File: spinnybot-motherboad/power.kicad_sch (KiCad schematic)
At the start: 19 parts, among them J11 POWER SW2, J9 POWER SW1, Q1 SISA96DN, Q2 SISA96DN, Q4 Q_NMOS_DGS, U1 LM1117-3.3

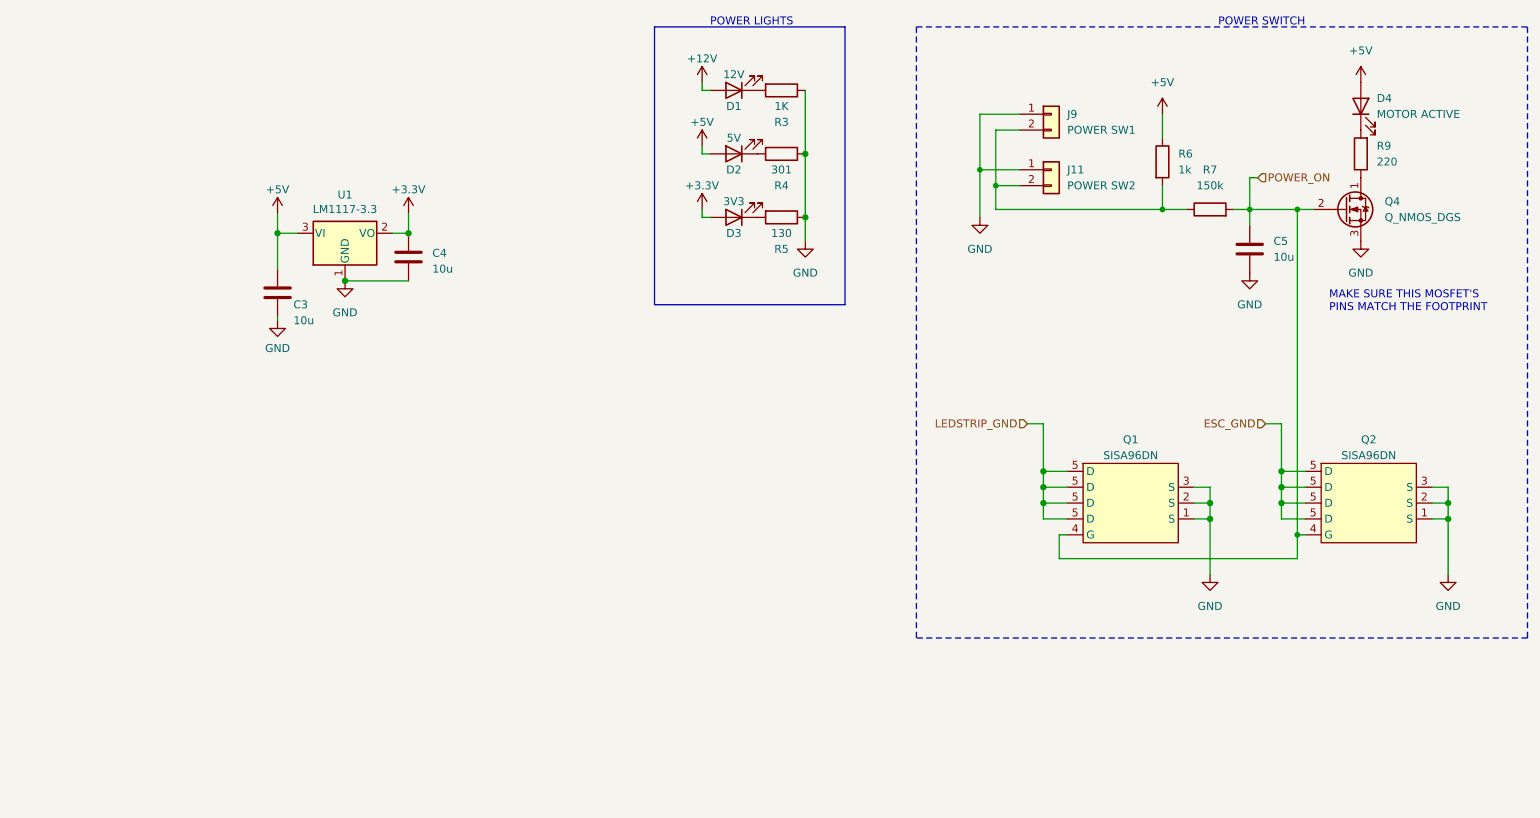
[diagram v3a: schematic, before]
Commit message: Power pads added, beginning routing
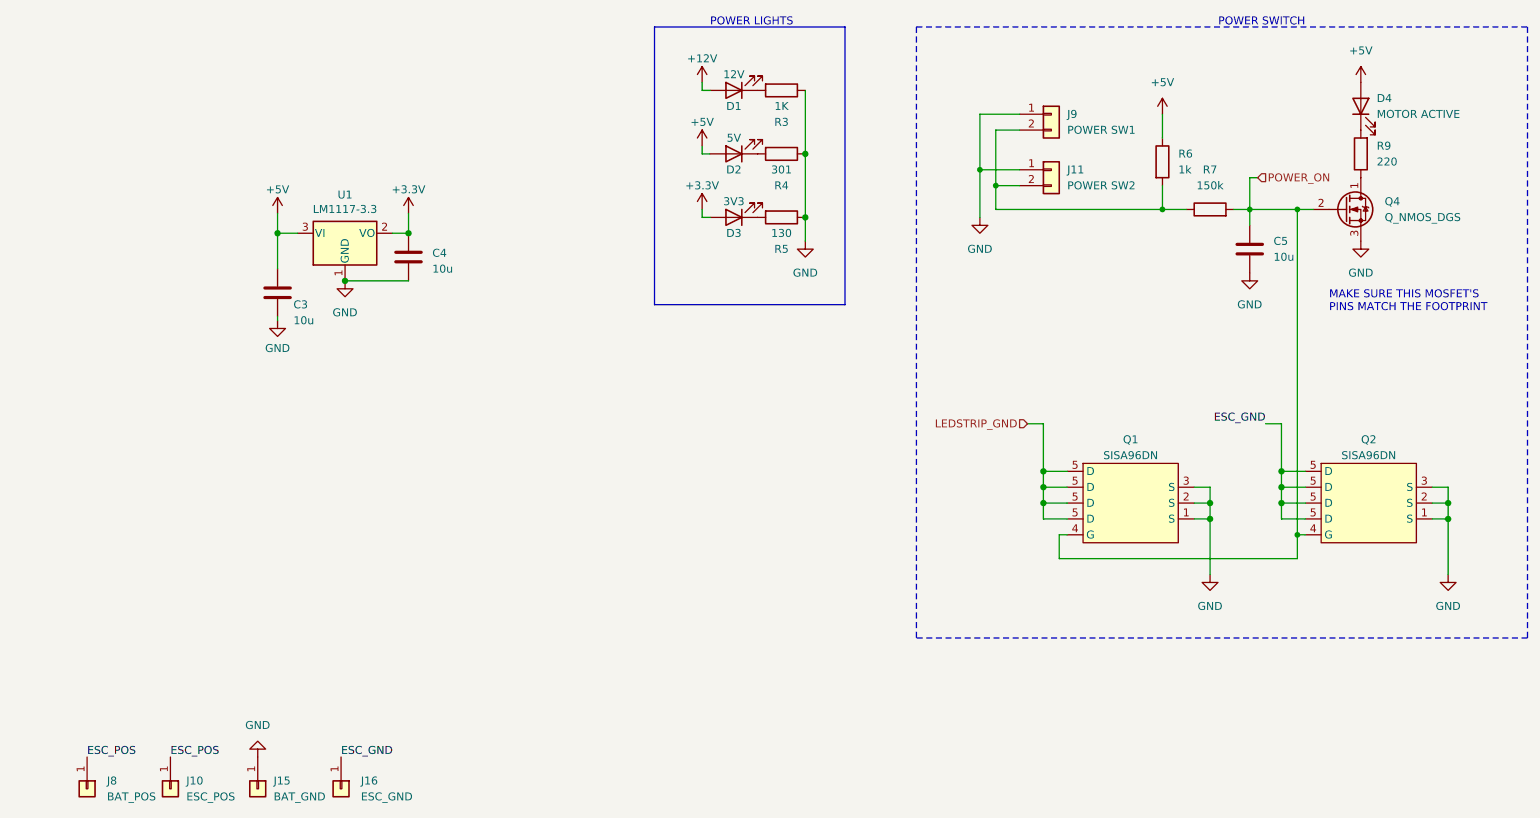
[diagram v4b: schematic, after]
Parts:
- added J10: ESC_POS, custom:Stitched_SolderWirePad_1x01_SMD_5x10mm, symbol Connector_Generic:Conn_01x01
- added J15: BAT_GND, custom:Stitched_SolderWirePad_1x01_SMD_5x10mm, symbol Connector_Generic:Conn_01x01
- added J16: ESC_GND, Connector_Wire:SolderWirePad_1x01_SMD_5x10mm, symbol Connector_Generic:Conn_01x01
- added J8: BAT_POS, Connector_Wire:SolderWirePad_1x01_SMD_5x10mm, symbol Connector_Generic:Conn_01x01
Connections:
- net ESC_GND: now also J16.1 (Pin_1)
- net GND: now also J15.1 (Pin_1)
- new net ESC_POS: J10.1 (Pin_1), J8.1 (Pin_1)
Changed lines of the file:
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@@
+    (effects (font (size 1.27 1.27)) (justify left bottom))
+  )
+  (label "ESC_POS" (at 40.005 134.62 0)
+    (effects (font (size 1.27 1.27)) (justify left bottom))
+  )
+  (label "ESC_GND" (at 80.645 134.62 0)
+    (effects (font (size 1.27 1.27)) (justify left bottom))
+  )
+  (label "ESC_GND" (at 228.6 81.28 180)
+    (effects (font (size 1.27 1.27)) (justify right bottom))
+  )
+  (label "ESC_POS" (at 53.34 134.62 0)
     (effects (font (size 1.27 1.27)) (justify left bottom))
   )
@@
     (effects (font (size 1.27 1.27)) (justify left))
   )
-  (hierarchical_label "ESC_GND" (shape input) (at 228.6 81.28 180)
-    (effects (font (size 1.27 1.27)) (justify right))
-  )
   (symbol (lib_id "power:GND") (at 219.71 105.41 0) (unit 1)
     (in_bom yes) (on_board yes)
@@
     )
     (property "Datasheet" "" (id 3) (at 70.485 47.625 0)
+      (effects (font (size 1.27 1.27)) hide)
+    )
+    (pin "1")
+  )
+  (symbol (lib_id "power:GND") (at 67.31 134.62 180) (unit 1)
+    (in_bom yes) (on_board yes) (fields_autoplaced)
+    (property "Reference" "#PWR0158" (id 0) (at 67.31 128.27 0)
+      (effects (font (size 1.27 1.27)) hide)
+    )
+    (property "Value" "GND" (id 1) (at 67.31 129.54 0))
+    (property "Footprint" "" (id 2) (at 67.31 134.62 0)
+      (effects (font (size 1.27 1.27)) hide)
+    )
+    (property "Datasheet" "" (id 3) (at 67.31 134.62 0)
+      (effects (font (size 1.27 1.27)) hide)
+    )
+    (pin "1")
+  )
+  (symbol (lib_id "Connector_Generic:Conn_01x01") (at 53.34 139.7 270) (unit 1)
+    (in_bom yes) (on_board yes) (fields_autoplaced)
+    (property "Reference" "J10" (id 0) (at 55.88 138.4299 90)
+      (effects (font (size 1.27 1.27)) (justify left))
+    )
+    (property "Value" "ESC_POS" (id 1) (at 55.88 140.9699 90)
+      (effects (font (size 1.27 1.27)) (justify left))
+    )
+    (property "Footprint" "custom:Stitched_SolderWirePad_1x01_SMD_5x10mm" (id 2) (at 53.34 139.7 0)
+      (effects (font (size 1.27 1.27)) hide)
+    )
+    (property "Datasheet" "~" (id 3) (at 53.34 139.7 0)
       (effects (font (size 1.27 1.27)) hide)
     )
@@
     )
     (property "Datasheet" "" (id 3) (at 212.09 31.75 0)
+      (effects (font (size 1.27 1.27)) hide)
+    )
+    (pin "1")
+  )
+  (symbol (lib_id "Connector_Generic:Conn_01x01") (at 67.31 139.7 270) (unit 1)
+    (in_bom yes) (on_board yes) (fields_autoplaced)
+    (property "Reference" "J15" (id 0) (at 69.85 138.4299 90)
+      (effects (font (size 1.27 1.27)) (justify left))
+    )
+    (property "Value" "BAT_GND" (id 1) (at 69.85 140.9699 90)
+      (effects (font (size 1.27 1.27)) (justify left))
+    )
+    (property "Footprint" "custom:Stitched_SolderWirePad_1x01_SMD_5x10mm" (id 2) (at 67.31 139.7 0)
+      (effects (font (size 1.27 1.27)) hide)
+    )
+    (property "Datasheet" "~" (id 3) (at 67.31 139.7 0)
       (effects (font (size 1.27 1.27)) hide)
     )
@@
     (pin "2")
   )
+  (symbol (lib_id "Connector_Generic:Conn_01x01") (at 40.005 139.7 270) (unit 1)
+    (in_bom yes) (on_board yes) (fields_autoplaced)
+    (property "Reference" "J8" (id 0) (at 43.18 138.4299 90)
+      (effects (font (size 1.27 1.27)) (justify left))
+    )
+    (property "Value" "BAT_POS" (id 1) (at 43.18 140.9699 90)
+      (effects (font (size 1.27 1.27)) (justify left))
+    )
+    (property "Footprint" "Connector_Wire:SolderWirePad_1x01_SMD_5x10mm" (id 2) (at 40.005 139.7 0)
+      (effects (font (size 1.27 1.27)) hide)
+    )
+    (property "Datasheet" "~" (id 3) (at 40.005 139.7 0)
+      (effects (font (size 1.27 1.27)) hide)
+    )
+    (pin "1")
+  )
   (symbol (lib_id "power:GND") (at 154.94 52.07 0) (unit 1)
     (in_bom yes) (on_board yes)
@@
     (pin "2")
   )
+  (symbol (lib_id "Connector_Generic:Conn_01x01") (at 80.645 139.7 270) (unit 1)
+    (in_bom yes) (on_board yes) (fields_autoplaced)
+    (property "Reference" "J16" (id 0) (at 83.82 138.4299 90)
+      (effects (font (size 1.27 1.27)) (justify left))
+    )
+    (property "Value" "ESC_GND" (id 1) (at 83.82 140.9699 90)
+      (effects (font (size 1.27 1.27)) (justify left))
+    )
+    (property "Footprint" "Connector_Wire:SolderWirePad_1x01_SMD_5x10mm" (id 2) (at 80.645 139.7 0)
+      (effects (font (size 1.27 1.27)) hide)
+    )
+    (property "Datasheet" "~" (id 3) (at 80.645 139.7 0)
+      (effects (font (size 1.27 1.27)) hide)
+    )
+    (pin "1")
+  )
   (symbol (lib_id "Device:C") (at 91.44 54.61 0) (unit 1)

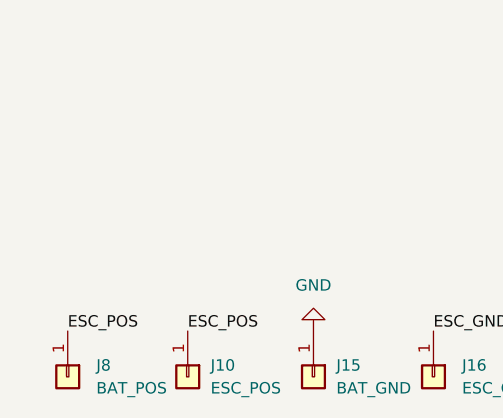
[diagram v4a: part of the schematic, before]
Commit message: Finishing routing board, needs checking over to make sure everything looks good
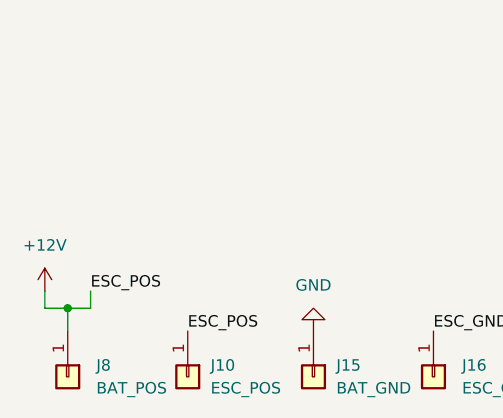
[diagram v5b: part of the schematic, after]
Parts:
- J11, J9: footprint Connector_JST:JST_PH_S2B-PH-SM4-TB_1x02-1MP_P2.00mm_Horizontal -> B2B-PH-SM4-TB(LF)(SN):B2B-PH-SM4-TBLFSN
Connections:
- net ESC_POS is gone; now on net +12V: J10.1 (Pin_1), J8.1 (Pin_1)
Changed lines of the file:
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@@
   (junction (at 212.09 46.99) (diameter 0) (color 0 0 0 0)
+  )
+  (junction (at 40.005 132.08) (diameter 0) (color 0 0 0 0)
   )
   (junction (at 182.88 40.64) (diameter 0) (color 0 0 0 0)
@@
     (stroke (width 0) (type default) (color 0 0 0 0))
   )
+  (wire (pts (xy 42.545 130.175) (xy 42.545 132.08))
+    (stroke (width 0) (type default) (color 0 0 0 0))
+  )
   (wire (pts (xy 154.94 48.26) (xy 154.94 52.07))
     (stroke (width 0) (type solid) (color 0 0 0 0))
   )
+  (wire (pts (xy 42.545 132.08) (xy 40.005 132.08))
+    (stroke (width 0) (type default) (color 0 0 0 0))
+  )
   (wire (pts (xy 217.17 93.98) (xy 219.71 93.98))
     (stroke (width 0) (type solid) (color 0 0 0 0))
@@
   )
   (wire (pts (xy 182.88 40.64) (xy 189.23 40.64))
+    (stroke (width 0) (type default) (color 0 0 0 0))
+  )
+  (wire (pts (xy 37.465 130.175) (xy 37.465 132.08))
     (stroke (width 0) (type default) (color 0 0 0 0))
   )
@@
     (stroke (width 0) (type solid) (color 0 0 0 0))
   )
+  (wire (pts (xy 40.005 132.08) (xy 37.465 132.08))
+    (stroke (width 0) (type default) (color 0 0 0 0))
+  )
   (wire (pts (xy 231.14 91.44) (xy 234.95 91.44))
     (stroke (width 0) (type solid) (color 0 0 0 0))
@@
   )
   (wire (pts (xy 189.23 31.75) (xy 182.88 31.75))
+    (stroke (width 0) (type default) (color 0 0 0 0))
+  )
+  (wire (pts (xy 40.005 134.62) (xy 40.005 132.08))
     (stroke (width 0) (type default) (color 0 0 0 0))
   )
@@
     (effects (font (size 1.27 1.27)) (justify left bottom))
   )
-  (label "ESC_POS" (at 40.005 134.62 0)
+  (label "ESC_POS" (at 42.545 130.175 0)
     (effects (font (size 1.27 1.27)) (justify left bottom))
   )
@@
       (effects (font (size 1.27 1.27)) (justify left))
     )
-    (property "Footprint" "Connector_JST:JST_PH_S2B-PH-SM4-TB_1x02-1MP_P2.00mm_Horizontal" (id 2) (at 194.31 40.64 0)
+    (property "Footprint" "B2B-PH-SM4-TB(LF)(SN):B2B-PH-SM4-TBLFSN" (id 2) (at 194.31 40.64 0)
       (effects (font (size 1.27 1.27)) hide)
     )
@@
     (pin "1")
     (pin "2")
+  )
+  (symbol (lib_id "power:+12V") (at 37.465 130.175 0) (unit 1)
+    (in_bom yes) (on_board yes) (fields_autoplaced)
+    (property "Reference" "#PWR0159" (id 0) (at 37.465 133.985 0)
+      (effects (font (size 1.27 1.27)) hide)
+    )
+    (property "Value" "+12V" (id 1) (at 37.465 125.095 0))
+    (property "Footprint" "" (id 2) (at 37.465 130.175 0)
+      (effects (font (size 1.27 1.27)) hide)
+    )
+    (property "Datasheet" "" (id 3) (at 37.465 130.175 0)
+      (effects (font (size 1.27 1.27)) hide)
+    )
+    (pin "1")
   )
   (symbol (lib_id "power:+3.3V") (at 138.43 46.99 0) (unit 1)
@@
       (effects (font (size 1.27 1.27)) (justify left))
     )
-    (property "Footprint" "Connector_JST:JST_PH_S2B-PH-SM4-TB_1x02-1MP_P2.00mm_Horizontal" (id 2) (at 194.31 31.75 0)
-      (effects (font (size 1.27 1.27)) hide)
-    )
+    (property "Footprint" "B2B-PH-SM4-TB(LF)(SN):B2B-PH-SM4-TBLFSN" (id 2) (at 194.31 31.75 0)
+      (effects (font (size 1.27 1.27)) hide)
+    )

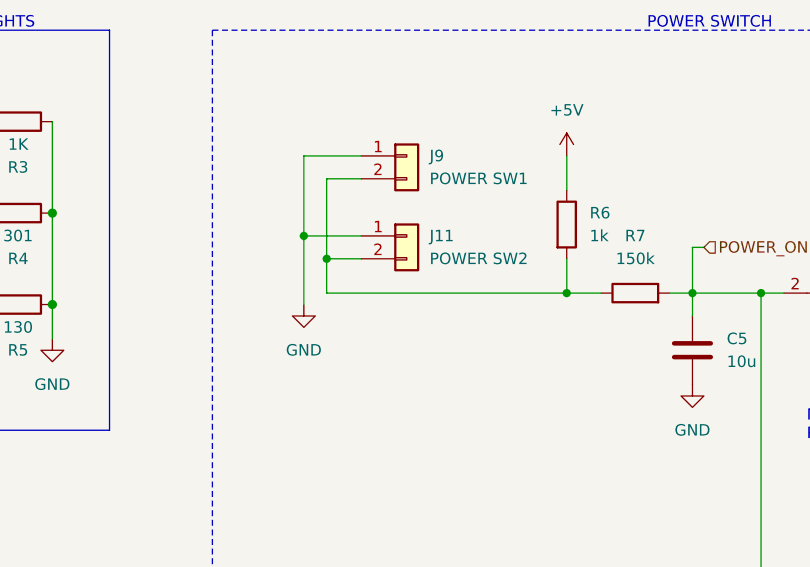
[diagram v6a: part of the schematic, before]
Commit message: tweaks to routing to make the ground plane more connected, add a top copper ground pour. move ESC FET.
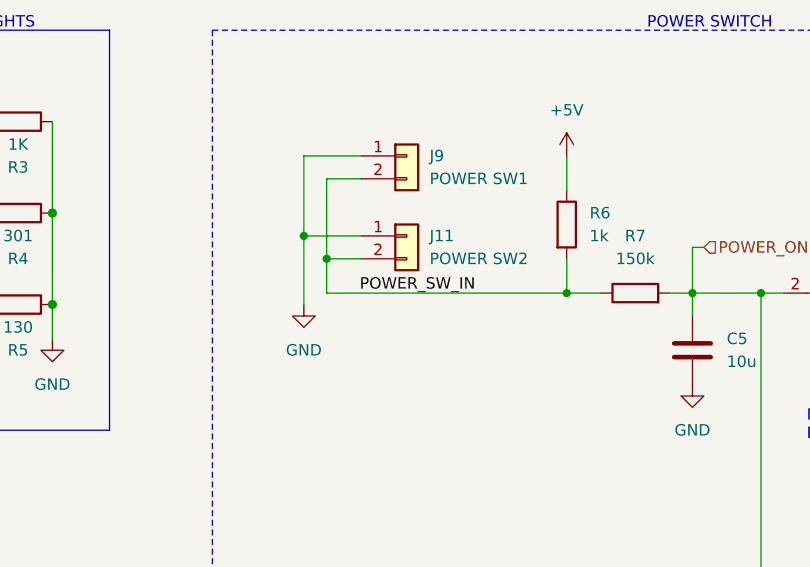
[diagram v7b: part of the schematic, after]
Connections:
- net POWER_SW_IN: now reaches J11.2 (Pin_2), J9.2 (Pin_2), R6.2, R7.1
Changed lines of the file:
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@@
     (effects (font (size 1.27 1.27)) (justify left bottom))
+  )
+  (label "POWER_SW_IN" (at 201.93 46.99 180)
+    (effects (font (size 1.27 1.27)) (justify right bottom))
   )
   (hierarchical_label "LEDSTRIP_GND" (shape input) (at 190.5 81.28 180)

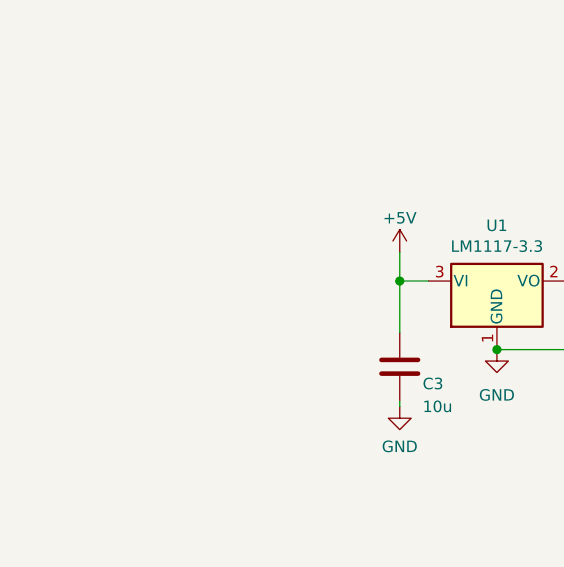
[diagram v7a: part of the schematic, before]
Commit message: add a couple ground test points
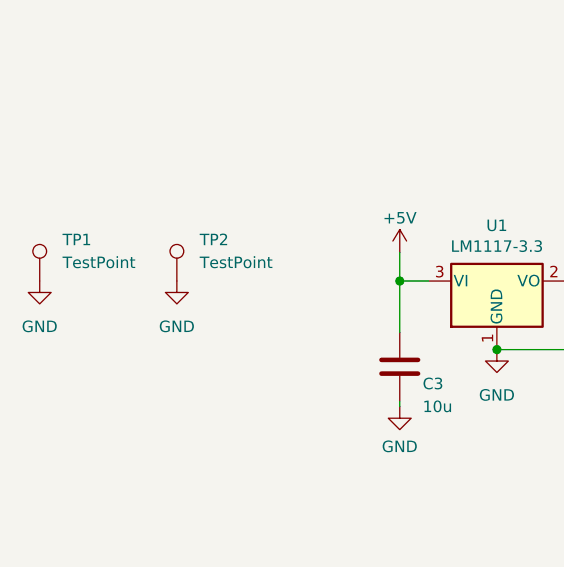
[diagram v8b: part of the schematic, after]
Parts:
- added TP1, TP2: TestPoint, TestPoint:TestPoint_Pad_D2.0mm, symbol Connector:TestPoint
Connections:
- net GND: now also TP1.1, TP2.1
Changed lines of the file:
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@@
     (pin "2")
+  )
+  (symbol (lib_id "power:GND") (at 45.72 50.8 0) (unit 1)
+    (in_bom yes) (on_board yes) (fields_autoplaced)
+    (property "Reference" "#PWR0169" (id 0) (at 45.72 57.15 0)
+      (effects (font (size 1.27 1.27)) hide)
+    )
+    (property "Value" "GND" (id 1) (at 45.72 55.88 0))
+    (property "Footprint" "" (id 2) (at 45.72 50.8 0)
+      (effects (font (size 1.27 1.27)) hide)
+    )
+    (property "Datasheet" "" (id 3) (at 45.72 50.8 0)
+      (effects (font (size 1.27 1.27)) hide)
+    )
+    (pin "1")
+  )
+  (symbol (lib_id "Connector:TestPoint") (at 45.72 50.8 0) (unit 1)
+    (in_bom yes) (on_board yes) (fields_autoplaced)
+    (property "Reference" "TP2" (id 0) (at 48.26 46.2279 0)
+      (effects (font (size 1.27 1.27)) (justify left))
+    )
+    (property "Value" "TestPoint" (id 1) (at 48.26 48.7679 0)
+      (effects (font (size 1.27 1.27)) (justify left))
+    )
+    (property "Footprint" "TestPoint:TestPoint_Pad_D2.0mm" (id 2) (at 50.8 50.8 0)
+      (effects (font (size 1.27 1.27)) hide)
+    )
+    (property "Datasheet" "~" (id 3) (at 50.8 50.8 0)
+      (effects (font (size 1.27 1.27)) hide)
+    )
+    (pin "1")
+  )
+  (symbol (lib_id "power:GND") (at 30.48 50.8 0) (unit 1)
+    (in_bom yes) (on_board yes) (fields_autoplaced)
+    (property "Reference" "#PWR0168" (id 0) (at 30.48 57.15 0)
+      (effects (font (size 1.27 1.27)) hide)
+    )
+    (property "Value" "GND" (id 1) (at 30.48 55.88 0))
+    (property "Footprint" "" (id 2) (at 30.48 50.8 0)
+      (effects (font (size 1.27 1.27)) hide)
+    )
+    (property "Datasheet" "" (id 3) (at 30.48 50.8 0)
+      (effects (font (size 1.27 1.27)) hide)
+    )
+    (pin "1")
   )
   (symbol (lib_id "Regulator_Linear:LM1117-3.3") (at 81.28 50.8 0) (unit 1)
@@
     (pin "2")
   )
+  (symbol (lib_id "Connector:TestPoint") (at 30.48 50.8 0) (unit 1)
+    (in_bom yes) (on_board yes) (fields_autoplaced)
+    (property "Reference" "TP1" (id 0) (at 33.02 46.2279 0)
+      (effects (font (size 1.27 1.27)) (justify left))
+    )
+    (property "Value" "TestPoint" (id 1) (at 33.02 48.7679 0)
+      (effects (font (size 1.27 1.27)) (justify left))
+    )
+    (property "Footprint" "TestPoint:TestPoint_Pad_D2.0mm" (id 2) (at 35.56 50.8 0)
+      (effects (font (size 1.27 1.27)) hide)
+    )
+    (property "Datasheet" "~" (id 3) (at 35.56 50.8 0)
+      (effects (font (size 1.27 1.27)) hide)
+    )
+    (pin "1")
+  )
   (symbol (lib_id "power:+3.3V") (at 91.44 47.625 0) (unit 1)
